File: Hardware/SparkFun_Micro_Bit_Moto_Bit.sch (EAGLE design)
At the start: 57 parts, among them J1 POWER_JACKPTH_LOCK, J10 Qwiic, J2 CORTEX_DEBUGPTH, U1 CY8C4245LQI-483, U2 TPS62172, U3 micro:bit, U4 DRV8835

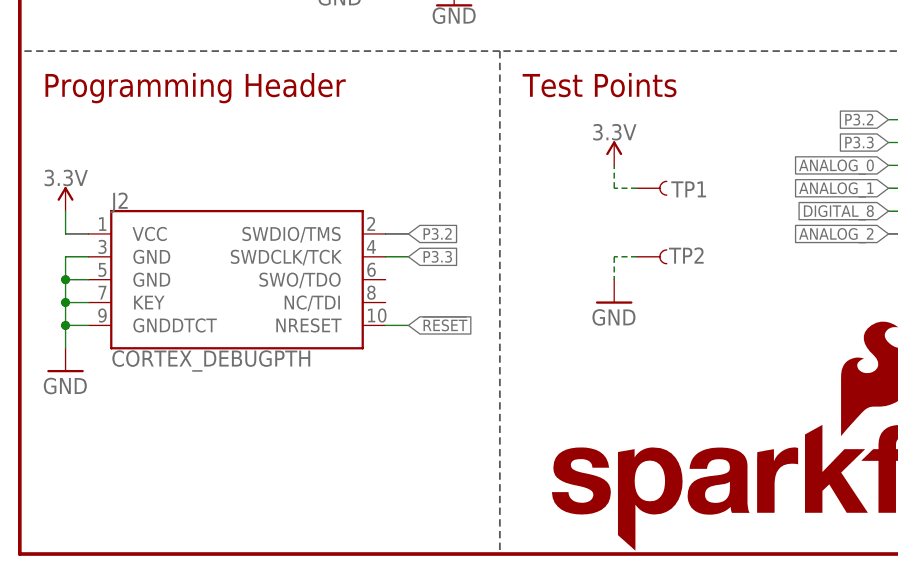
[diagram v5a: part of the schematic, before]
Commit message: Design review changes
Moved test points to line up with TB pogo pins
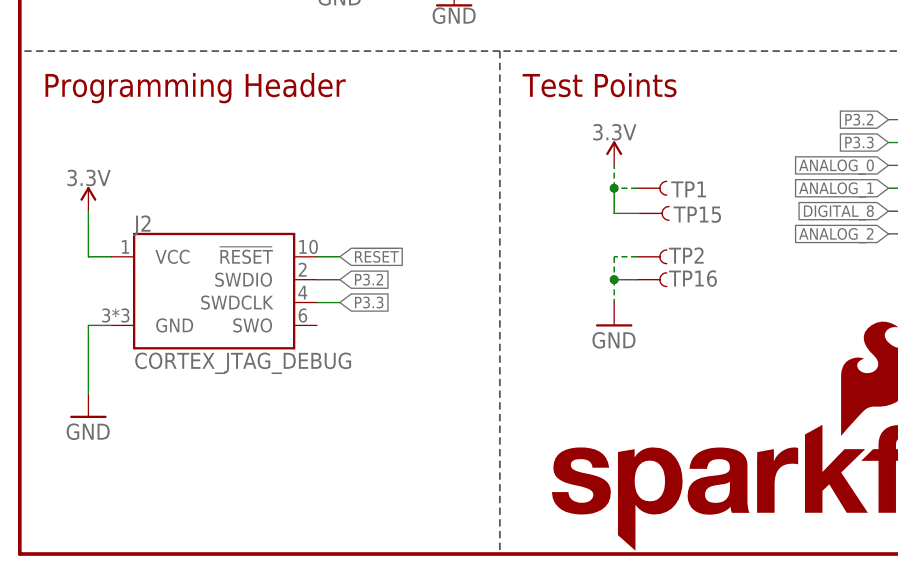
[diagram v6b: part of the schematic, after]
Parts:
- added TP15, TP16: TEST-POINT3, SparkFun-Connectors:TEST-POINT3
- J2: value CORTEX_DEBUGPTH -> CORTEX_JTAG_DEBUG; device Pete_Connectors_Retired:CORTEX_DEBUGPTH -> SparkFun-Connectors:CORTEX_JTAG_DEBUG_MINIMUM_PTH_NS
- TP10, TP11, TP12, TP13, TP14, TP5, TP6, TP7, TP8, TP9: value TEST-POINTTP_15TH_THRU -> TEST-POINT3; device SparkFun-Connectors:TEST-POINTTP_15TH_THRU -> SparkFun-Connectors:TEST-POINT3
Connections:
- net !RESET: now also J2.!RESET; no longer J2.NRESET
- net 3.3V: now also TP15.1
- net GND: now also J2.GND, TP16.1; no longer J2.GND@3, J2.GND@5, J2.GNDDTCT, J2.KEY
- net P3.2: now also J2.SWDIO; no longer J2.SWDIO/TMS
- net P3.3: now also J2.SWDCLK; no longer J2.SWDCLK/TCK
